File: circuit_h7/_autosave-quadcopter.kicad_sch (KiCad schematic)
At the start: 112 parts, among them J1 Conn_01x04_Male, J10 Conn_01x01_Female, J11 Conn_01x04_Male, J12 Conn_01x04_Male, J13 Conn_01x01_Female, J14 Conn_01x01_Female, J16 Conn_01x01_Female, J17 Conn_01x01_Female, J18 USB_C_Receptacle_USB2.0, J19 Conn_01x08_Male, J2 Conn_01x01_Female, J21 Conn_01x01_Female, J22 Conn_01x01_Female, J23 Conn_01x01_Female, J24 Conn_01x01_Female, J25 Conn_01x01_Female, J26 Conn_01x01_Female, J28 Conn_01x01_Female, J29 Conn_01x01_Female, J3 Conn_01x01_Female, J30 Conn_01x01_Female, J31 Conn_01x01_Female, J32 Conn_01x01_Female, J33 Conn_01x01_Female, J37 Conn_01x01_Female, J4 Conn_01x01_Female, J40 Conn_01x01_Female, J41 Conn_01x01_Female, J42 Conn_01x01_Female, J43 Conn_01x01_Female, J44 Conn_01x01_Female, J45 Conn_01x01_Female, J47 Conn_01x01_Female, J48 Conn_01x01_Female, J49 Conn_01x01_Female, J5 Conn_Coaxial, J50 Conn_01x01_Female, J6 Conn_01x06_Male, J7 Conn_01x01_Female, J8 Conn_01x01_Female, J9 Conn_01x01_Female, Q1 AO3400A, SW1 SW_DIP_x01, U1 STM32H723VGH6, U2 ICM-42605, U3 DPS310, U4 3V3, U5 EUP3458 1.2A, 30V max input, 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, U6 2450FM07D0034T, U7 W25Q80DVUXIE TR (16M), U8 SX1281, U9 5v, 500mA, Y1 16M, Y2 52Mhz, 12pF

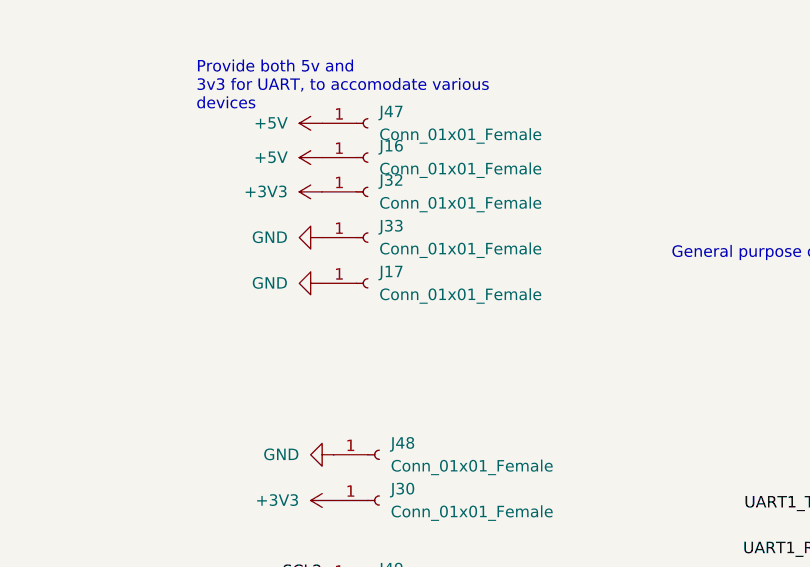
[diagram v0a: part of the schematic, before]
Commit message: Set up ADC measurements
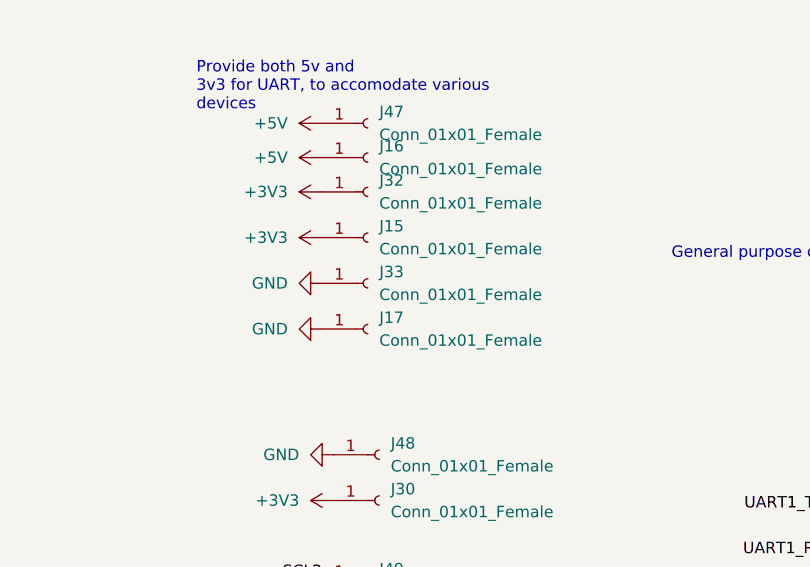
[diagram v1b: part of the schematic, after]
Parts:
- added J15: Conn_01x01_Female, TestPoint:TestPoint_Pad_2.0x2.0mm, symbol Connector:Conn_01x01_Female
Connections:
- net +3V3: now also J15.1 (Pin_1)
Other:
- moved on the sheet: J17, J33
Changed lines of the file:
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@@
     (pin "2")
   )
-  (symbol (lib_id "power:GND") (at 325.12 185.42 270) (unit 1)
-    (in_bom yes) (on_board yes) (fields_autoplaced)
-    (property "Reference" "#PWR0161" (id 0) (at 318.77 185.42 0)
-      (effects (font (size 1.27 1.27)) hide)
-    )
-    (property "Value" "GND" (id 1) (at 321.31 185.4199 90)
-      (effects (font (size 1.27 1.27)) (justify right))
-    )
-    (property "Footprint" "" (id 2) (at 325.12 185.42 0)
-      (effects (font (size 1.27 1.27)) hide)
-    )
-    (property "Datasheet" "" (id 3) (at 325.12 185.42 0)
+  (symbol (lib_id "power:GND") (at 325.12 190.5 270) (unit 1)
+    (in_bom yes) (on_board yes) (fields_autoplaced)
+    (property "Reference" "#PWR0161" (id 0) (at 318.77 190.5 0)
+      (effects (font (size 1.27 1.27)) hide)
+    )
+    (property "Value" "GND" (id 1) (at 321.31 190.4999 90)
+      (effects (font (size 1.27 1.27)) (justify right))
+    )
+    (property "Footprint" "" (id 2) (at 325.12 190.5 0)
+      (effects (font (size 1.27 1.27)) hide)
+    )
+    (property "Datasheet" "" (id 3) (at 325.12 190.5 0)
       (effects (font (size 1.27 1.27)) hide)
     )
@@
     (pin "1")
   )
-  (symbol (lib_id "power:GND") (at 325.12 180.34 270) (unit 1)
-    (in_bom yes) (on_board yes) (fields_autoplaced)
-    (property "Reference" "#PWR0141" (id 0) (at 318.77 180.34 0)
-      (effects (font (size 1.27 1.27)) hide)
-    )
-    (property "Value" "GND" (id 1) (at 321.31 180.3399 90)
-      (effects (font (size 1.27 1.27)) (justify right))
-    )
-    (property "Footprint" "" (id 2) (at 325.12 180.34 0)
-      (effects (font (size 1.27 1.27)) hide)
-    )
-    (property "Datasheet" "" (id 3) (at 325.12 180.34 0)
+  (symbol (lib_id "power:GND") (at 325.12 185.42 270) (unit 1)
+    (in_bom yes) (on_board yes) (fields_autoplaced)
+    (property "Reference" "#PWR0141" (id 0) (at 318.77 185.42 0)
+      (effects (font (size 1.27 1.27)) hide)
+    )
+    (property "Value" "GND" (id 1) (at 321.31 185.4199 90)
+      (effects (font (size 1.27 1.27)) (justify right))
+    )
+    (property "Footprint" "" (id 2) (at 325.12 185.42 0)
+      (effects (font (size 1.27 1.27)) hide)
+    )
+    (property "Datasheet" "" (id 3) (at 325.12 185.42 0)
       (effects (font (size 1.27 1.27)) hide)
     )
@@
     (pin "2")
   )
+  (symbol (lib_id "Connector:Conn_01x01_Female") (at 330.2 180.34 0) (unit 1)
+    (in_bom yes) (on_board yes) (fields_autoplaced)
+    (property "Reference" "J15" (id 0) (at 331.47 179.0699 0)
+      (effects (font (size 1.27 1.27)) (justify left))
+    )
+    (property "Value" "Conn_01x01_Female" (id 1) (at 331.47 181.6099 0)
+      (effects (font (size 1.27 1.27)) (justify left))
+    )
+    (property "Footprint" "TestPoint:TestPoint_Pad_2.0x2.0mm" (id 2) (at 330.2 180.34 0)
+      (effects (font (size 1.27 1.27)) hide)
+    )
+    (property "Datasheet" "~" (id 3) (at 330.2 180.34 0)
+      (effects (font (size 1.27 1.27)) hide)
+    )
+    (pin "1")
+  )
   (symbol (lib_id "power:GND") (at 284.48 219.71 180) (unit 1)
     (in_bom yes) (on_board yes)
@@
     (pin "1")
   )
+  (symbol (lib_id "power:+3V3") (at 325.12 180.34 90) (unit 1)
+    (in_bom yes) (on_board yes) (fields_autoplaced)
+    (property "Reference" "#PWR0166" (id 0) (at 328.93 180.34 0)
+      (effects (font (size 1.27 1.27)) hide)
+    )
+    (property "Value" "+3V3" (id 1) (at 321.31 180.3399 90)
+      (effects (font (size 1.27 1.27)) (justify left))
+    )
+    (property "Footprint" "" (id 2) (at 325.12 180.34 0)
+      (effects (font (size 1.27 1.27)) hide)
+    )
+    (property "Datasheet" "" (id 3) (at 325.12 180.34 0)
+      (effects (font (size 1.27 1.27)) hide)
+    )
+    (pin "1")
+  )
   (symbol (lib_id "power:GND") (at 504.19 109.22 270) (unit 1)
     (in_bom yes) (on_board yes) (fields_autoplaced)
@@
     (pin "1")
   )
-  (symbol (lib_id "Connector:Conn_01x01_Female") (at 330.2 180.34 0) (unit 1)
-    (in_bom yes) (on_board yes) (fields_autoplaced)
-    (property "Reference" "J33" (id 0) (at 331.47 179.0699 0)
-      (effects (font (size 1.27 1.27)) (justify left))
-    )
-    (property "Value" "Conn_01x01_Female" (id 1) (at 331.47 181.6099 0)
-      (effects (font (size 1.27 1.27)) (justify left))
-    )
-    (property "Footprint" "TestPoint:TestPoint_Pad_2.0x2.0mm" (id 2) (at 330.2 180.34 0)
-      (effects (font (size 1.27 1.27)) hide)
-    )
-    (property "Datasheet" "~" (id 3) (at 330.2 180.34 0)
+  (symbol (lib_id "Connector:Conn_01x01_Female") (at 330.2 185.42 0) (unit 1)
+    (in_bom yes) (on_board yes) (fields_autoplaced)
+    (property "Reference" "J33" (id 0) (at 331.47 184.1499 0)
+      (effects (font (size 1.27 1.27)) (justify left))
+    )
+    (property "Value" "Conn_01x01_Female" (id 1) (at 331.47 186.6899 0)
+      (effects (font (size 1.27 1.27)) (justify left))
+    )
+    (property "Footprint" "TestPoint:TestPoint_Pad_2.0x2.0mm" (id 2) (at 330.2 185.42 0)
+      (effects (font (size 1.27 1.27)) hide)
+    )
+    (property "Datasheet" "~" (id 3) (at 330.2 185.42 0)
       (effects (font (size 1.27 1.27)) hide)
     )
@@
     (pin "2")
   )
-  (symbol (lib_id "Connector:Conn_01x01_Female") (at 330.2 185.42 0) (unit 1)
-    (in_bom yes) (on_board yes) (fields_autoplaced)
-    (property "Reference" "J17" (id 0) (at 331.47 184.1499 0)
-      (effects (font (size 1.27 1.27)) (justify left))
-    )
-    (property "Value" "Conn_01x01_Female" (id 1) (at 331.47 186.6899 0)
-      (effects (font (size 1.27 1.27)) (justify left))
-    )
-    (property "Footprint" "TestPoint:TestPoint_Pad_2.0x2.0mm" (id 2) (at 330.2 185.42 0)
-      (effects (font (size 1.27 1.27)) hide)
-    )
-    (property "Datasheet" "~" (id 3) (at 330.2 185.42 0)
+  (symbol (lib_id "Connector:Conn_01x01_Female") (at 330.2 190.5 0) (unit 1)
+    (in_bom yes) (on_board yes) (fields_autoplaced)
+    (property "Reference" "J17" (id 0) (at 331.47 189.2299 0)
+      (effects (font (size 1.27 1.27)) (justify left))
+    )
+    (property "Value" "Conn_01x01_Female" (id 1) (at 331.47 191.7699 0)
+      (effects (font (size 1.27 1.27)) (justify left))
+    )
+    (property "Footprint" "TestPoint:TestPoint_Pad_2.0x2.0mm" (id 2) (at 330.2 190.5 0)
+      (effects (font (size 1.27 1.27)) hide)
+    )
+    (property "Datasheet" "~" (id 3) (at 330.2 190.5 0)
       (effects (font (size 1.27 1.27)) hide)
     )
@@
       (reference "#PWR0165") (unit 1) (value "GND") (footprint "")
     )
+    (path "/dafa6052-5cc9-4f6f-b13f-0ea391dfb9df"
+      (reference "#PWR0166") (unit 1) (value "+3V3") (footprint "")
+    )
     (path "/6c03fa7b-8858-4fff-8684-a4780ff0bd25"
       (reference "#PWR0167") (unit 1) (value "GND") (footprint "")
@@
       (reference "J14") (unit 1) (value "Conn_01x01_Female") (footprint "TestPoint:TestPoint_Pad_2.0x2.0mm")
     )
+    (path "/a3301b96-cdeb-4af7-9814-7aae6fb00f00"
+      (reference "J15") (unit 1) (value "Conn_01x01_Female") (footprint "TestPoint:TestPoint_Pad_2.0x2.0mm")
+    )
     (path "/17cad9ea-946e-421b-a91a-894f3c7195f4"
